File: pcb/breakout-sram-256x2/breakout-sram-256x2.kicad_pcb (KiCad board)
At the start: 4 copper layers, 62 x 62 mm, 11 parts, among them J1 FX18-120P-0.8SV20, J2 FX18-120S-0.8SV20, U1 IS61WV25616-10TLI, U3 IS61WV25616-10TLI

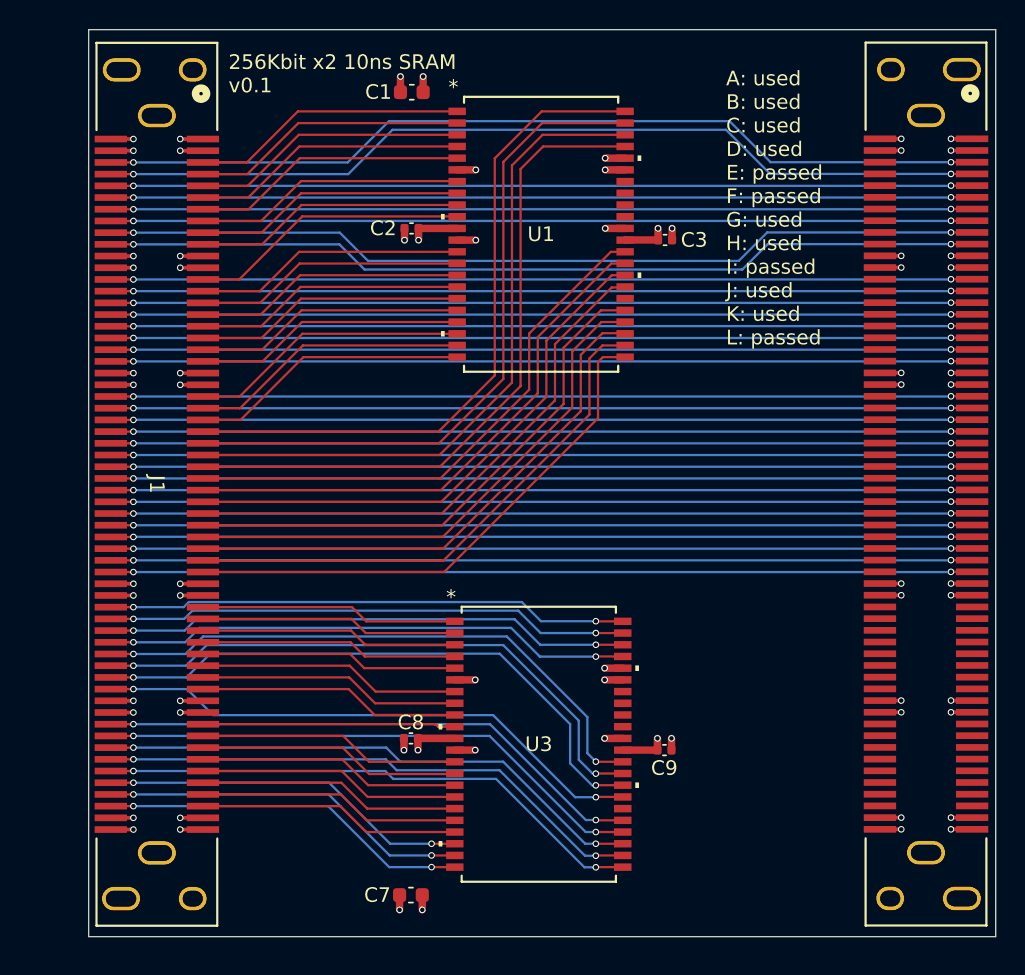
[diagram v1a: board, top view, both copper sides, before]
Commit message: [axi][sram] set jlcpcb rotation
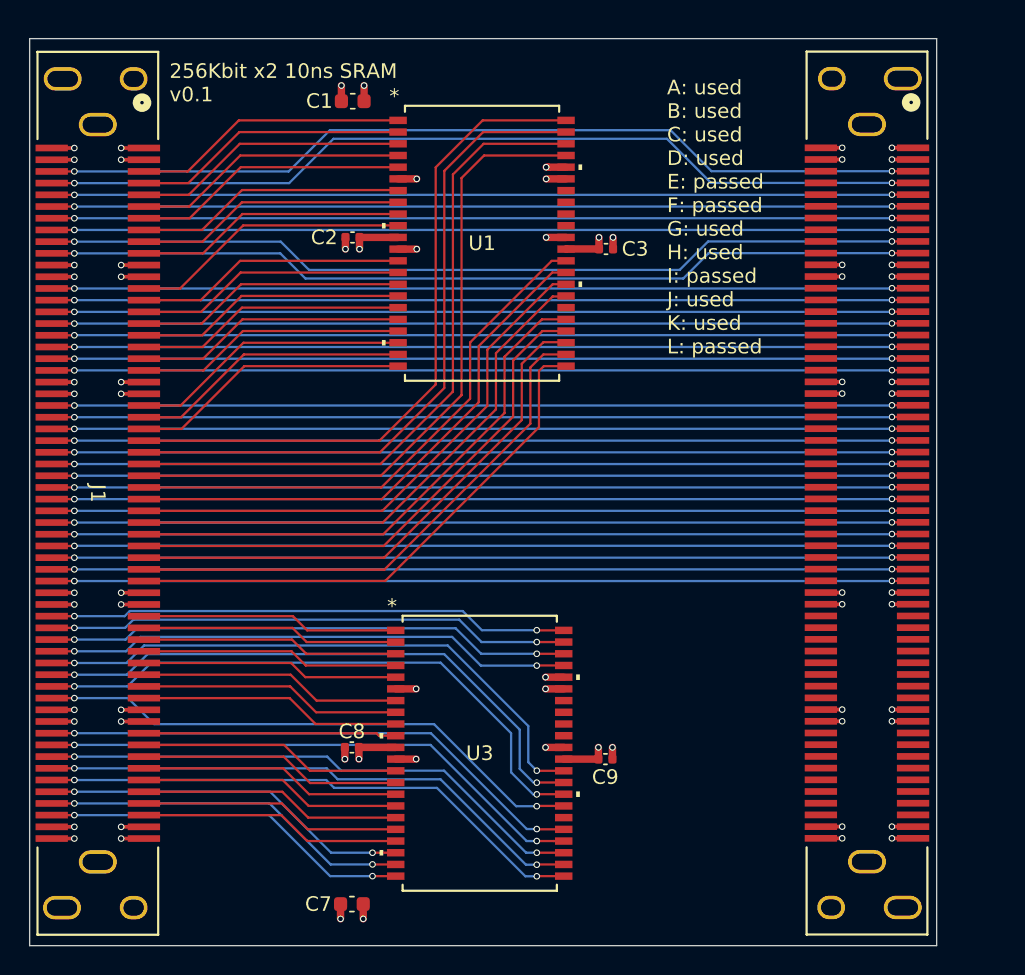
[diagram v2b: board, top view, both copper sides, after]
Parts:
- removed REF**: OSHW-Logo2_14.6x12mm_SilkScreen, Symbol:OSHW-Logo2_14.6x12mm_SilkScreen
- moved C8 4.08 mm to (69.1, 90.6)
- moved C1 4.08 mm to (69.2, 46.4)
- moved C7 4.08 mm to (69.1, 101.3)
- moved C9 4.08 mm to (86.5, 91.4)
- moved J1 4.08 mm to (51.8, 73.2)
- moved J2 4.08 mm to (104.3, 73.2)
- moved U3 4.08 mm to (77.9, 91.0)
- moved C2 4.08 mm to (69.2, 55.7)
- moved C3 4.08 mm to (86.5, 56.5)
- moved U1 4.08 mm to (78.0, 56.1)
